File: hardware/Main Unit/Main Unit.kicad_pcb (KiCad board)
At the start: 2 copper layers, 79 parts, among them J1 3221-10-0300-00, J10 DM3AT, J2 61801525123, J3 61801525123, J4 61801525123, J5 61801525123, J6 61801525123, J7 61801525123, J8 61801525123, J9 61801525123, SW1 MJTP1243, SW2 MJTP1243, U1 MCXN547VKLT, U2 TLV71333PDBV, U3 SN74CB3Q3257PWR, U4 SN74CB3Q3257PWR, U5 SN74CB3Q3257PWR, U6 SN74CB3Q3257PWR, U7 74AHC1G04, U8 AP22913W6-7, U9 SN74AXC4T774, X1 24.0000MHz

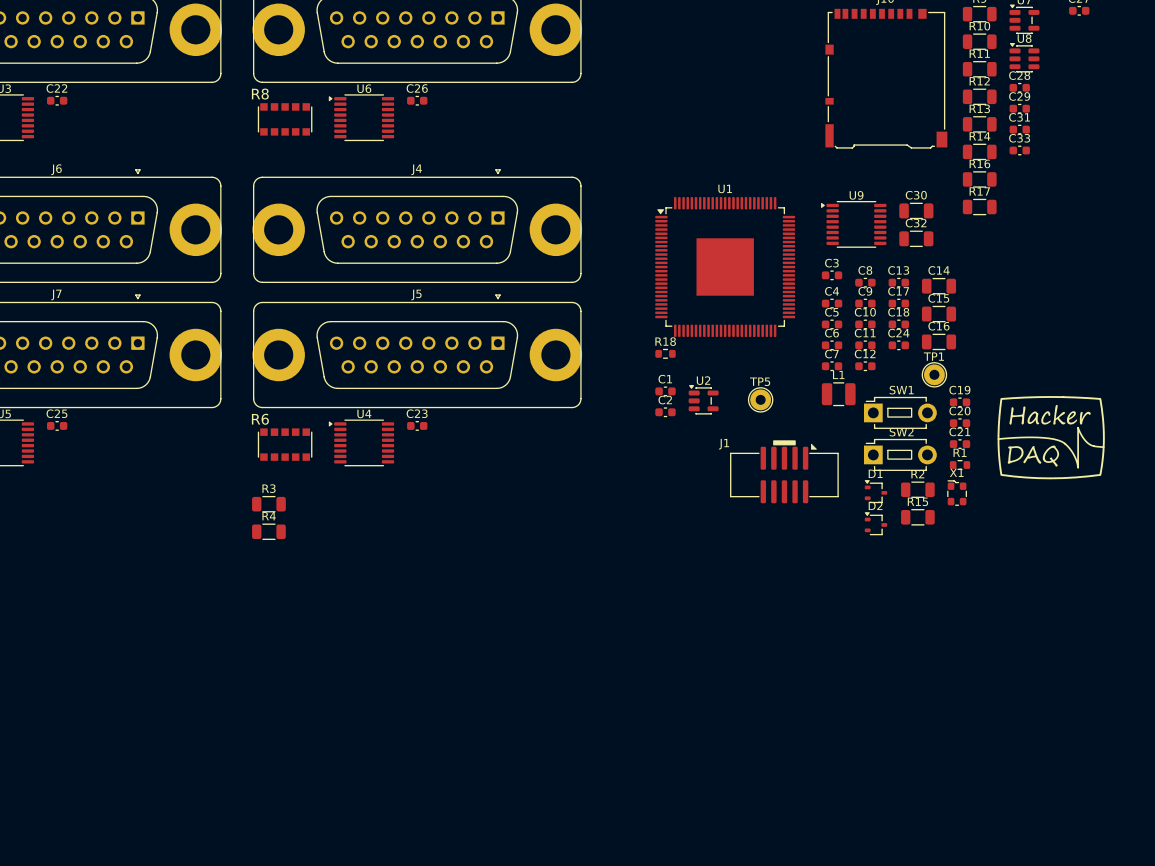
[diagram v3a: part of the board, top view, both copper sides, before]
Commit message: Implement Ethernet, start on voltage regulator
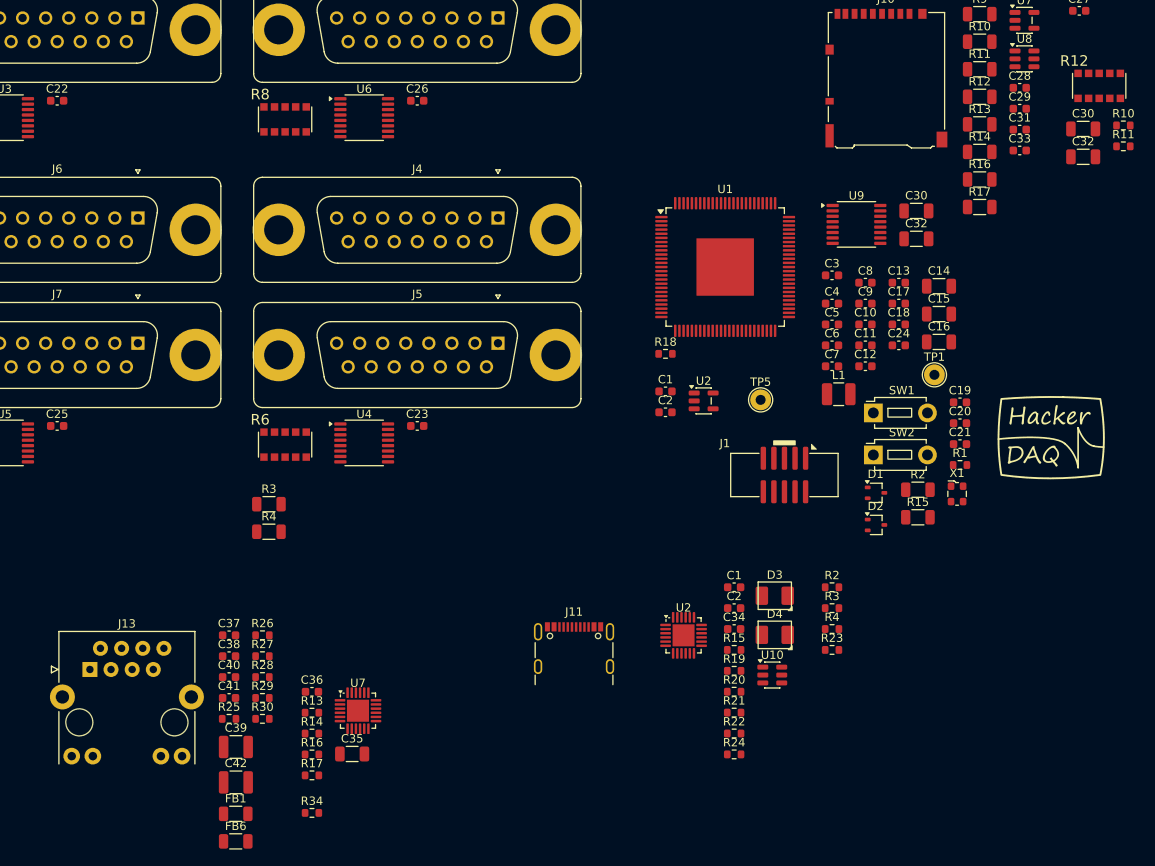
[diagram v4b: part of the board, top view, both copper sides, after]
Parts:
- added C1: 1µF, Capacitor_SMD:C_0603_1608Metric, F.Cu at (161.9, 138.5)
- added C2: 100nF, Capacitor_SMD:C_0603_1608Metric, F.Cu at (161.9, 141.0)
- added C30: 10µF, Capacitor_SMD:C_1206_3216Metric, F.Cu at (203.8, 83.4)
- added C32: 10µF, Capacitor_SMD:C_1206_3216Metric, F.Cu at (203.8, 86.8)
- added C34: 100nF, Capacitor_SMD:C_0603_1608Metric, F.Cu at (161.9, 143.5)
- added C35: 2.2µF, Capacitor_SMD:C_1206_3216Metric, F.Cu at (116.0, 158.5)
- added C36: 100nF, Capacitor_SMD:C_0603_1608Metric, F.Cu at (111.2, 151.0)
- added C37: 100nF, Capacitor_SMD:C_0603_1608Metric, F.Cu at (101.2, 144.2)
- added C38: 100nF, Capacitor_SMD:C_0603_1608Metric, F.Cu at (101.2, 146.8)
- added C39: 22µF, Capacitor_SMD:C_1210_3225Metric, F.Cu at (102.1, 157.7)
- added C40: 100nF, Capacitor_SMD:C_0603_1608Metric, F.Cu at (101.2, 149.3)
- added C41: 100nF, Capacitor_SMD:C_0603_1608Metric, F.Cu at (101.2, 151.8)
- added C42: 22µF, Capacitor_SMD:C_1210_3225Metric, F.Cu at (102.1, 161.9)
- added D3: AA3528SYSK, ColorLEDs:AA3528, F.Cu at (166.8, 139.5)
- added D4: AA3528QBS, ColorLEDs:AA3528, F.Cu at (166.8, 144.2)
- added FB1: 300@100MHz, Resistor_SMD:R_1206_3216Metric, F.Cu at (102.0, 165.7)
- added FB6: 300@100MHz, Resistor_SMD:R_1206_3216Metric, F.Cu at (102.0, 169.0)
- added J11: USB4105-GF-A, Project Library:USB_C_Receptacle_GCT_USB4105-xx-A_16P_TopMnt_Horizontal-ExtraHoleClearance, F.Cu at (142.7, 146.9)
- added J13: HFJ11-2450E-L21RL, Project Library:RJ45_HALO_HFJ11-x2450E-LxxRL_Horizontal-Fixed3DModel, F.Cu at (84.5, 148.3)
- added R10: 10k, Resistor_SMD:R_0603_1608Metric, F.Cu at (208.7, 83.0)
- added R11: 10k, Resistor_SMD:R_0603_1608Metric, F.Cu at (208.7, 85.5)
- added R12: 10k, Project Library:CTS 745C101, F.Cu at (205.8, 78.2)
- added R13: 33, Resistor_SMD:R_0603_1608Metric, F.Cu at (111.2, 153.5)
- added R14: 33, Resistor_SMD:R_0603_1608Metric, F.Cu at (111.2, 156.1)
- added R15: 5.1k, Resistor_SMD:R_0603_1608Metric, F.Cu at (161.9, 146.0)
- added R16: 33, Resistor_SMD:R_0603_1608Metric, F.Cu at (111.2, 158.6)
- added R17: 33, Resistor_SMD:R_0603_1608Metric, F.Cu at (111.2, 161.1)
- added R19: 5.1k, Resistor_SMD:R_0603_1608Metric, F.Cu at (161.9, 148.5)
- added R2: 10k, Resistor_SMD:R_0603_1608Metric, F.Cu at (173.7, 138.5)
- added R20: 140, Resistor_SMD:R_0603_1608Metric, F.Cu at (161.9, 151.0)
- added R21: 30, Resistor_SMD:R_0603_1608Metric, F.Cu at (161.9, 153.5)
- added R22: 10k, Resistor_SMD:R_0603_1608Metric, F.Cu at (161.9, 156.0)
- added R23: 10k, Resistor_SMD:R_0603_1608Metric, F.Cu at (173.7, 146.0)
- added R24: 4.7k, Resistor_SMD:R_0603_1608Metric, F.Cu at (161.9, 158.6)
- added R25: 4.7k, Resistor_SMD:R_0603_1608Metric, F.Cu at (101.2, 154.3)
- added R26: 270, Resistor_SMD:R_0603_1608Metric, F.Cu at (105.2, 144.2)
- added R27: 270, Resistor_SMD:R_0603_1608Metric, F.Cu at (105.2, 146.8)
- added R28: 10k, Resistor_SMD:R_0603_1608Metric, F.Cu at (105.2, 149.3)
- added R29: 10k, Resistor_SMD:R_0603_1608Metric, F.Cu at (105.2, 151.8)
- added R3: 10k, Resistor_SMD:R_0603_1608Metric, F.Cu at (173.7, 141.0)
- added R30: 6.49k, Resistor_SMD:R_0603_1608Metric, F.Cu at (105.2, 154.3)
- added R34: 33, Resistor_SMD:R_0603_1608Metric, F.Cu at (111.2, 165.6)
- added R4: 10k, Resistor_SMD:R_0603_1608Metric, F.Cu at (173.7, 143.5)
- added U10: USBLC6-2SC6, Package_TO_SOT_SMD:SOT-23-6, F.Cu at (166.5, 149.0)
- added U2: CY7C65223, Project Library:QFN-24-1EP_4x4mm_P0.5mm_EP2.65x2.65mm-LengthenedPads, F.Cu at (155.8, 144.2)
- added U7: KSZ8081RND, Project Library:QFN-24-1EP_4x4mm_P0.5mm_EP2.65x2.65mm-LengthenedPads, F.Cu at (116.7, 153.3)
- U1: footprint Package_QFP:LQFP-100-1EP_14x14mm_P0.5mm_EP6.9x6.9mm -> Project Library:LQFP-100-1EP_14x14mm_P0.5mm_EP6.9x6.9mm_Fixed3DModel
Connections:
- net /MCU/ETH_RMII.MDIO renamed /ETH_RMII.MDIO
- C19 pad 1: /MCU/~{RST} -> /~{MCU_RST}
- D1 pad 1: /MCU/~{RST} -> /~{MCU_RST}
- J1 pad 10: /MCU/~{RST} -> /~{MCU_RST}
- R1 pad 1: /MCU/~{RST} -> /~{MCU_RST}
- SW1 pad 2: /MCU/~{RST} -> /~{MCU_RST}
- U1 pad 100: /MCU/ETH_RMII.TXD1 -> /ETH_RMII.TXD1
- U1 pad 35: unconnected-(U1E-P4_12-Pad35) -> /DBG_UART.MCU_RX
- U1 pad 36: unconnected-(U1E-P4_13-Pad36) -> /DBG_UART.MCU_TX
- U1 pad 48: unconnected-(U1E-P5_0-Pad48) -> /~{ETH_SPEED_LED}
- U1 pad 49: unconnected-(U1E-P5_1-Pad49) -> /~{SD_CARD_EN}
- U1 pad 5: /MCU/ETH_RMII.RX_ER -> /ETH_RMII.RX_ER
- U1 pad 6: /MCU/ETH_RMII.CRS_DV -> /ETH_RMII.CRS_DV
- U1 pad 67: /MCU/uSD_SPI_FC6.~{CS} -> /uSD_SPI.~{CS}
- U1 pad 68: /MCU/uSD_SPI_FC6.MISO -> /uSD_SPI.MISO
- U1 pad 7: /MCU/ETH_RMII.RXD0 -> /ETH_RMII.RXD0
- U1 pad 72: /MCU/uSD_SPI_FC6.SCLK -> /uSD_SPI.SCLK
- U1 pad 74: /MCU/uSD_SPI_FC6.MOSI -> /uSD_SPI.MOSI
- U1 pad 8: /MCU/ETH_RMII.RXD1 -> /ETH_RMII.RXD1
- U1 pad 94: /MCU/ETH_RMII.MDC -> /ETH_RMII.MDC
- U1 pad 97: /MCU/ETH_RMII.RMII_CLK -> /ETH_RMII.RMII_CLK
- U1 pad 98: /MCU/ETH_RMII.TX_EN -> /ETH_RMII.TX_EN
- U1 pad 99: /MCU/ETH_RMII.TXD0 -> /ETH_RMII.TXD0
- U7 pad 1: (no net) -> unconnected-(U7-NC-Pad1)
- U9 pad 3: /MicroSDCard/SPI.~{CS} -> /uSD_SPI.~{CS}
- U9 pad 4: /MicroSDCard/SPI.MOSI -> /uSD_SPI.MOSI
- U9 pad 5: /MicroSDCard/SPI.SCLK -> /uSD_SPI.SCLK
- U9 pad 6: /MicroSDCard/SPI.MISO -> Net-(U9-A4)
- U9 pad 9: /MicroSDCard/~SD_CARD_ENABLE -> /~{SD_CARD_EN}

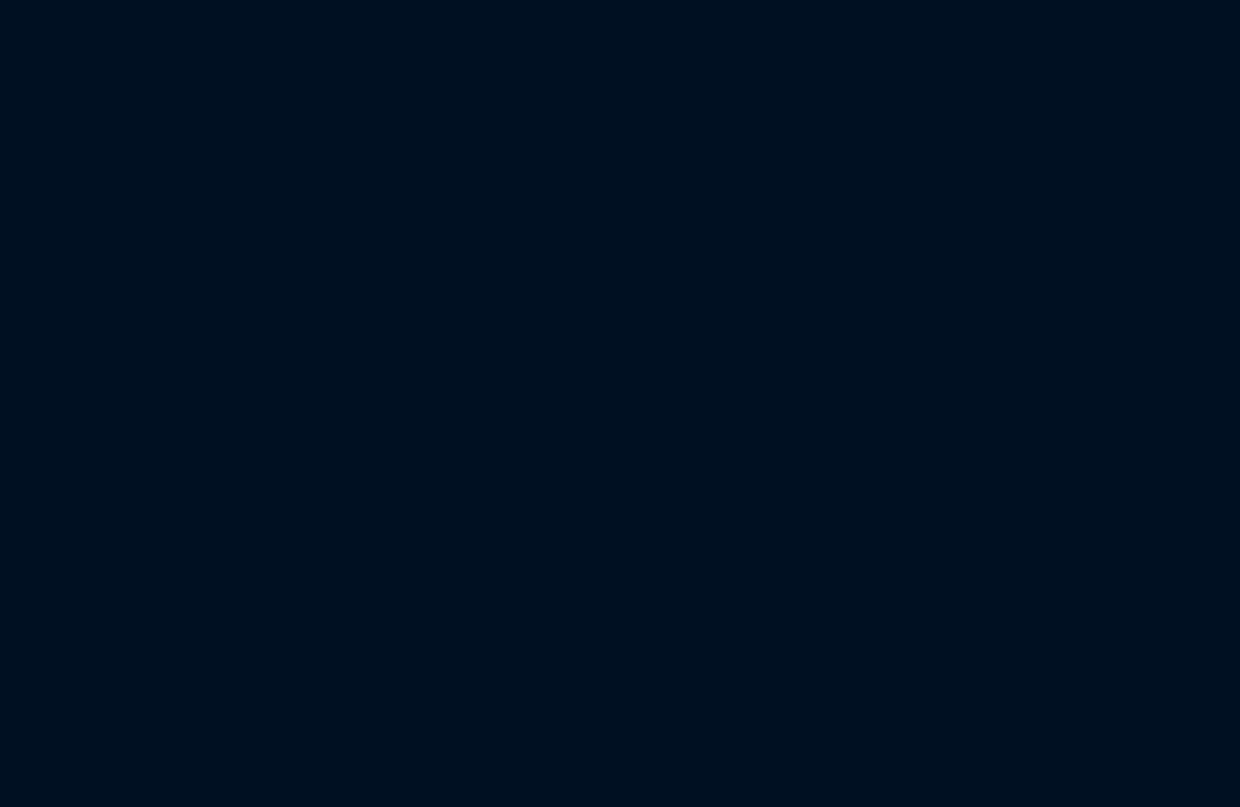
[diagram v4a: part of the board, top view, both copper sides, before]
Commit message: Finish 3.3V regulator
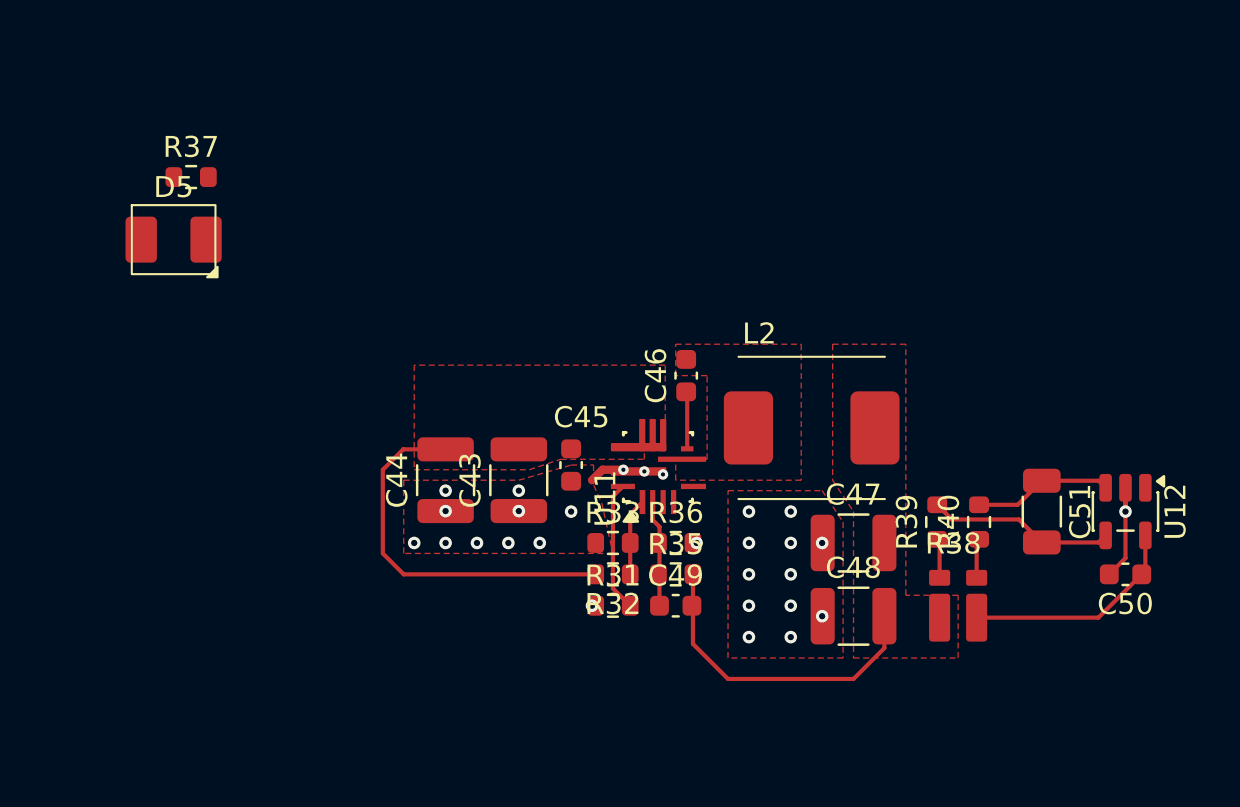
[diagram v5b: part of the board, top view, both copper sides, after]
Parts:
- added C43: 10µF, Capacitor_SMD:C_1210_3225Metric, F.Cu at (238.0, 112.5)
- added C44: 10µF, Capacitor_SMD:C_1210_3225Metric, F.Cu at (234.5, 112.5)
- added C45: 100nF, Capacitor_SMD:C_0603_1608Metric, F.Cu at (240.5, 111.8)
- added C46: 100nF, Capacitor_SMD:C_0603_1608Metric, F.Cu at (246.0, 107.5)
- added C47: 22µF, Capacitor_SMD:C_1210_3225Metric, F.Cu at (254.0, 115.5)
- added C48: 22µF, Capacitor_SMD:C_1210_3225Metric, F.Cu at (254.0, 119.0)
- added C49: 150pF, Capacitor_SMD:C_0603_1608Metric, F.Cu at (245.5, 118.5)
- added C50: 100nF, Capacitor_SMD:C_0603_1608Metric, F.Cu at (267.0, 117.0)
- added C51: 10µF, Capacitor_SMD:C_1206_3216Metric, F.Cu at (263.0, 114.0)
- added D5: AA3528CGSK, ColorLEDs:AA3528, F.Cu at (221.5, 101.0)
- added L2: 2.2μH, Project Library:0630CDMCDDS, F.Cu at (252.0, 110.0)
- added R31: 52.3k, Resistor_SMD:R_0603_1608Metric, F.Cu at (242.5, 118.5)
- added R32: 18.2k, Resistor_SMD:R_0603_1608Metric, F.Cu at (242.5, 117.0)
- added R33: 3.01k, Resistor_SMD:R_0603_1608Metric, F.Cu at (242.5, 115.5)
- added R35: 45.3k, Resistor_SMD:R_0603_1608Metric, F.Cu at (245.5, 117.0)
- added R36: 10k, Resistor_SMD:R_0603_1608Metric, F.Cu at (245.5, 115.5)
- added R37: 140, Resistor_SMD:R_0603_1608Metric, F.Cu at (222.3, 98.0)
- added R38: .0025, Project Library:D1FCP0612, F.Cu at (259.0, 117.2)
- added R39: 10, Resistor_SMD:R_0603_1608Metric, F.Cu at (258.0, 114.5)
- added R40: 10, Resistor_SMD:R_0603_1608Metric, F.Cu at (260.0, 114.5)
- added U11: TPS56A37RPAR, Project Library:RPA0010A-MFG, F.Cu at (244.6, 111.9)
- added U12: INA180A3, Package_TO_SOT_SMD:SOT-23-5, F.Cu at (267.0, 114.0)
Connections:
- net /uSD_SPI.MISO renamed /MCU/uSD_SPI_FC6.MISO
- net /uSD_SPI.MOSI renamed /MCU/uSD_SPI_FC6.MOSI
- net /uSD_SPI.SCLK renamed /MCU/uSD_SPI_FC6.SCLK
- net /uSD_SPI.~{CS} renamed /MCU/uSD_SPI_FC6.~{CS}
- net /~{MCU_RST} renamed /EthernetInterface/~{RST}
- net /~{SD_CARD_EN} renamed /MCU/~{SD_CARD_EN}
- J2 pad 1: /Card Bus Connectors0/V_SUPPLY -> V_{SUPPLY}
- J3 pad 1: /Card Bus Connectors0/V_SUPPLY -> V_{SUPPLY}
- J4 pad 1: /Card Bus Connectors1/V_SUPPLY -> V_{SUPPLY}
- J5 pad 1: /Card Bus Connectors1/V_SUPPLY -> V_{SUPPLY}
- J6 pad 1: /Card Bus Connectors2/V_SUPPLY -> V_{SUPPLY}
- J7 pad 1: /Card Bus Connectors2/V_SUPPLY -> V_{SUPPLY}
- J8 pad 1: /Card Bus Connectors3/V_SUPPLY -> V_{SUPPLY}
- J9 pad 1: /Card Bus Connectors3/V_SUPPLY -> V_{SUPPLY}
- U1 pad 37: unconnected-(U1E-P4_15-Pad37) -> /+3.3V_CUR_SENSE
- U1 pad 38: unconnected-(U1E-P4_16-Pad38) -> /MCU/+5V_CUR_SENSE
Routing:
- net V_{SUPPLY}: track 0.00 -> 18.0 mm
- net /SupplyTo3.3VRegulator/+3.3V_PRE_SENSE: track 0.00 -> 15.3 mm
- net +3.3V: track 0.00 -> 10.7 mm
- net Net-(U12--): track 0.00 -> 8.94 mm
- net GND: track 0.00 -> 7.30 mm, vias 0 -> 28
- net Net-(U12-+): track 0.00 -> 6.67 mm
- net Net-(U11-MODE): track 0.00 -> 6.24 mm
- net /SupplyTo3.3VRegulator/FB: track 0.00 -> 5.09 mm
- net /SupplyTo3.3VRegulator/EN: track 0.00 -> 3.70 mm
- net /SupplyTo3.3VRegulator/BOOT: track 0.00 -> 2.75 mm
- net Net-(R38-Pad3): track 0.00 -> 1.89 mm
- net Net-(R38-Pad2): track 0.00 -> 1.89 mm
- added copper zone on F.Cu, net /SupplyTo3.3VRegulator/+3.3V_PRE_SENSE
- added copper zone on F.Cu, net /SupplyTo3.3VRegulator/SW
- added copper zone on F.Cu, net GND
- added copper zone on F.Cu, net V_{SUPPLY}
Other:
- copper layers 2 -> 4
